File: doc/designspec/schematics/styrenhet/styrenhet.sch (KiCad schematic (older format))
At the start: 7 parts, among them IC1 ATMEGA1284P-P, U1 IQEXO-3, U2 Terminator-CTRL, U3 USB-UART

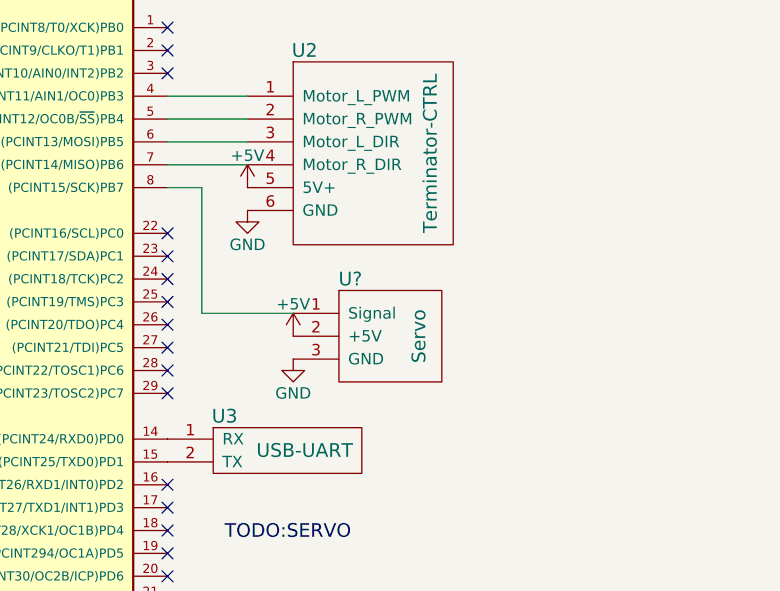
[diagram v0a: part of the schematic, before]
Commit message: Add JTAG programmer
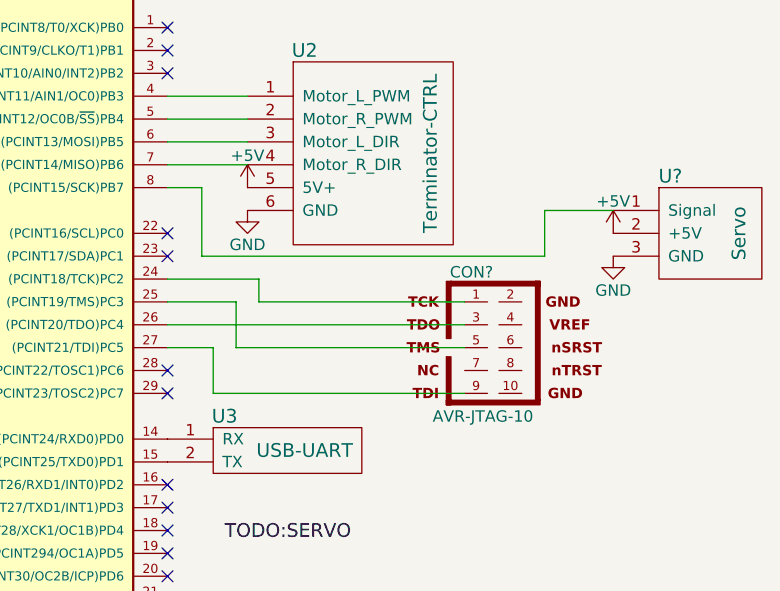
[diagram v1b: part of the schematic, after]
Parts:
- added CON?: AVR-JTAG-10, AVR-JTAG-10, symbol AVR-JTAG-10
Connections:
- net at IC1.24 ((PCINT18/TCK)PC2): now also CON?.1
- net at IC1.25 ((PCINT19/TMS)PC3): now also CON?.5
- net at IC1.26 ((PCINT20/TDO)PC4): now also CON?.3
- net at IC1.27 ((PCINT21/TDI)PC5): now also CON?.9
- no-connect marks 28 -> 24
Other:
- moved on the sheet: U?
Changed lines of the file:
@@
 NoConn ~ 5750 3800
 NoConn ~ 5750 3900
-NoConn ~ 5750 4000
-NoConn ~ 5750 4100
-NoConn ~ 5750 4200
-NoConn ~ 5750 4300
 NoConn ~ 5750 4400
 NoConn ~ 5750 4500
@@
 Wire Wire Line
 	5750 3600 5900 3600
-Wire Wire Line
-	5900 3600 5900 4150
-Wire Wire Line
-	5900 4150 6300 4150
 $Comp
 L Servo U?
 U 1 1 57FFAFE2
-P 6850 4250
-F 0 "U?" H 6550 4500 60  0000 C CNN
-F 1 "Servo" V 6850 4250 60  0000 C CNN
-F 2 "" H 6850 4250 60  0001 C CNN
-F 3 "" H 6850 4250 60  0001 C CNN
-	1    6850 4250
+P 8250 3800
+F 0 "U?" H 7950 4050 60  0000 C CNN
+F 1 "Servo" V 8250 3800 60  0000 C CNN
+F 2 "" H 8250 3800 60  0001 C CNN
+F 3 "" H 8250 3800 60  0001 C CNN
+	1    8250 3800
 	1    0    0    -1
 $EndComp
@@
 L +5V #PWR?
 U 1 1 57FFB033
-P 6300 4250
-F 0 "#PWR?" H 6300 4100 50  0001 C CNN
-F 1 "+5V" H 6300 4390 50  0000 C CNN
-F 2 "" H 6300 4250 50  0000 C CNN
-F 3 "" H 6300 4250 50  0000 C CNN
-	1    6300 4250
+P 7700 3800
+F 0 "#PWR?" H 7700 3650 50  0001 C CNN
+F 1 "+5V" H 7700 3940 50  0000 C CNN
+F 2 "" H 7700 3800 50  0000 C CNN
+F 3 "" H 7700 3800 50  0000 C CNN
+	1    7700 3800
 	1    0    0    -1
 $EndComp
@@
 L GND #PWR?
 U 1 1 57FFB05B
-P 6300 4350
-F 0 "#PWR?" H 6300 4100 50  0001 C CNN
-F 1 "GND" H 6300 4200 50  0000 C CNN
-F 2 "" H 6300 4350 50  0000 C CNN
-F 3 "" H 6300 4350 50  0000 C CNN
-	1    6300 4350
+P 7700 3900
+F 0 "#PWR?" H 7700 3650 50  0001 C CNN
+F 1 "GND" H 7700 3750 50  0000 C CNN
+F 2 "" H 7700 3900 50  0000 C CNN
+F 3 "" H 7700 3900 50  0000 C CNN
+	1    7700 3900
 	1    0    0    -1
 $EndComp
@@
 Wire Wire Line
 	3700 2000 3750 2000
+$Comp
+L AVR-JTAG-10 CON?
+U 1 1 5803B292
+P 7250 4300
+F 0 "CON?" H 7080 4630 50  0000 C CNN
+F 1 "AVR-JTAG-10" H 6910 3970 50  0000 L BNN
+F 2 "AVR-JTAG-10" V 6680 4320 50  0001 C CNN
+F 3 "" H 7250 4300 50  0000 C CNN
+	1    7250 4300
+	1    0    0    -1
+$EndComp
+Wire Wire Line
+	5900 3600 5900 3900
+Wire Wire Line
+	5900 3900 7400 3900
+Wire Wire Line
+	7400 3900 7400 3700
+Wire Wire Line
+	7400 3700 7700 3700
+Wire Wire Line
+	7050 4100 6150 4100
+Wire Wire Line
+	6150 4100 6150 4000
+Wire Wire Line
+	6150 4000 5750 4000
+Wire Wire Line
+	7050 4200 5750 4200
+Wire Wire Line
+	7050 4300 6050 4300
+Wire Wire Line
+	6050 4300 6050 4100
+Wire Wire Line
+	6050 4100 5750 4100
+Wire Wire Line
+	7050 4500 5950 4500
+Wire Wire Line
+	5950 4500 5950 4300
+Wire Wire Line
+	5950 4300 5750 4300
 $EndSCHEMATC

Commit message: Use button for reset
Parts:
- removed SW?: SPST, symbol SPST
- added SW?: SW_PUSH, symbol SW_PUSH
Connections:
- net GND: now also SW?.1
- net RESET: now also SW?.2
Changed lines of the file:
@@
-$EndComp
-$Comp
-L SPST SW?
-U 1 1 58011D2C
-P 2000 1400
-F 0 "SW?" H 2000 1500 50  0000 C CNN
-F 1 "SPST" H 2000 1300 50  0000 C CNN
-F 2 "" H 2000 1400 50  0000 C CNN
-F 3 "" H 2000 1400 50  0000 C CNN
-	1    2000 1400
-	1    0    0    -1
 $EndComp
 $Comp
@@
 L GND #PWR?
 U 1 1 58011E31
-P 1500 1400
-F 0 "#PWR?" H 1500 1150 50  0001 C CNN
-F 1 "GND" H 1500 1250 50  0000 C CNN
-F 2 "" H 1500 1400 50  0000 C CNN
-F 3 "" H 1500 1400 50  0000 C CNN
-	1    1500 1400
+P 1900 1400
+F 0 "#PWR?" H 1900 1150 50  0001 C CNN
+F 1 "GND" H 1900 1250 50  0000 C CNN
+F 2 "" H 1900 1400 50  0000 C CNN
+F 3 "" H 1900 1400 50  0000 C CNN
+	1    1900 1400
 	1    0    0    -1
 $EndComp
@@
 Wire Wire Line
 	5950 4300 5750 4300
+$Comp
+L SW_PUSH SW?
+U 1 1 5804FD05
+P 2200 1400
+F 0 "SW?" H 2350 1510 50  0000 C CNN
+F 1 "SW_PUSH" H 2200 1320 50  0000 C CNN
+F 2 "" H 2200 1400 50  0000 C CNN
+F 3 "" H 2200 1400 50  0000 C CNN
+	1    2200 1400
+	1    0    0    -1
+$EndComp
 $EndSCHEMATC
